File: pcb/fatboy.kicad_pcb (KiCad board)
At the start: 2 copper layers, 232.2 x 108.2 mm, 78 parts, among them J1 Conn_01x04, SW1 SW_Push, U1 Helios

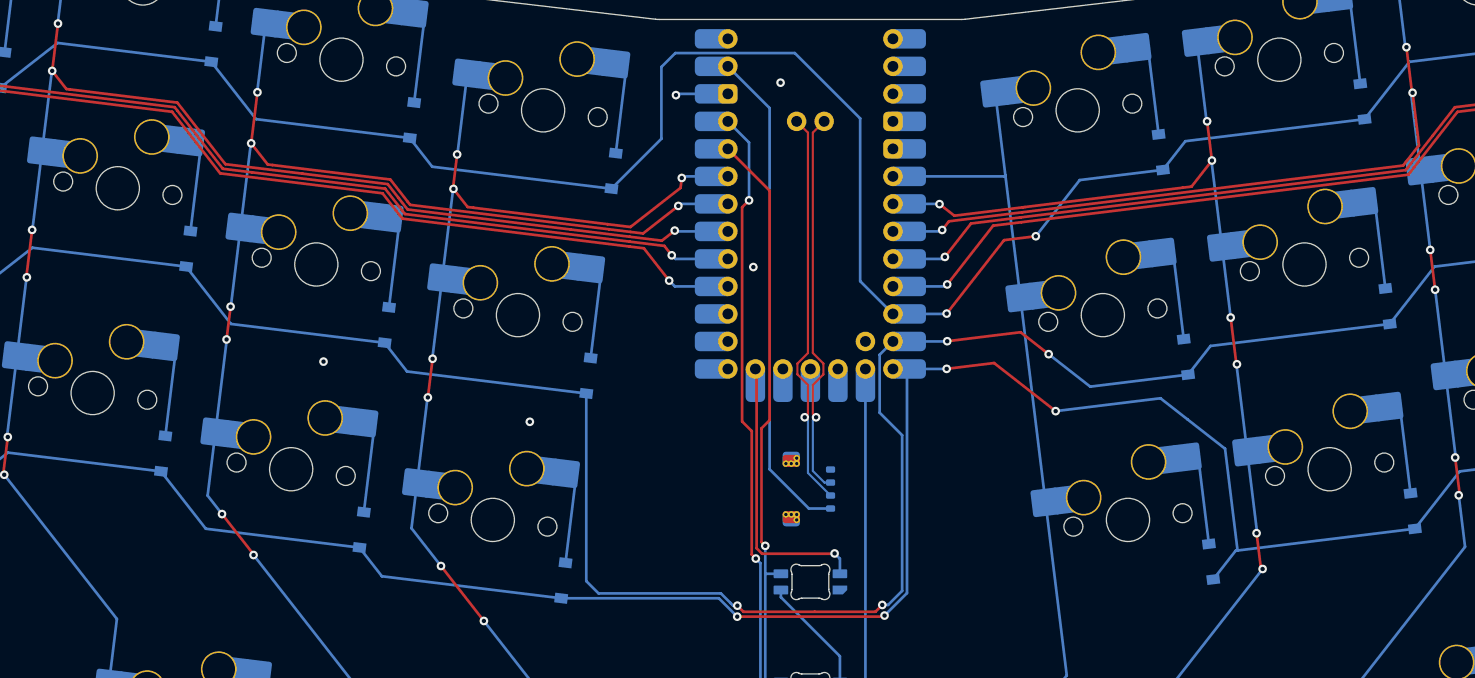
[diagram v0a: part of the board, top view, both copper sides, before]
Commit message: pcb: remove daughterboard
Signed-off-by: Anant Thazhemadam <anant.thazhemadam@gmail.com>
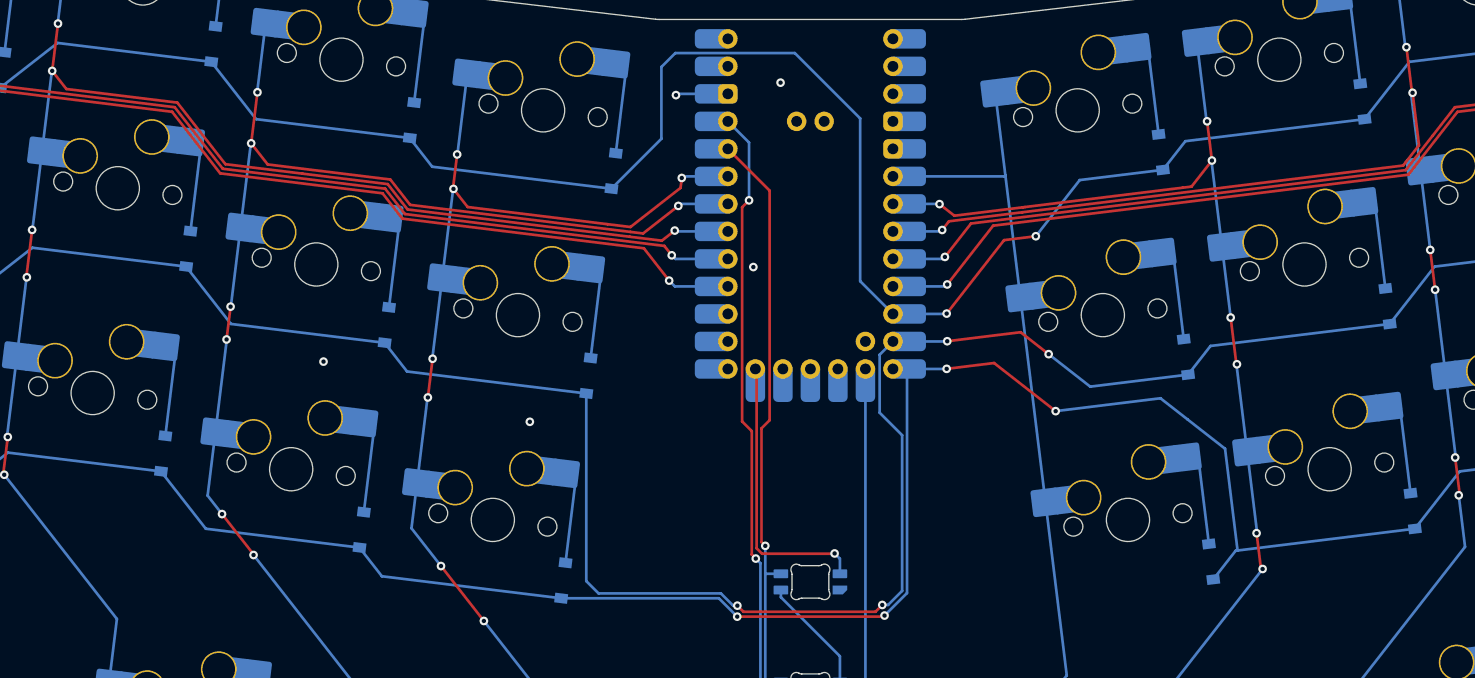
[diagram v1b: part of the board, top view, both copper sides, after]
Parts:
- removed J1: Conn_01x04, fatboy:Molex_Pico-EZmate_78171-0004_1x04-1MP_P1.20mm_Vertical
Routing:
- net 5V: track 45.9 -> 0.00 mm
- net D-: track 36.9 -> 0.00 mm, vias 1 -> 0
- net D+: track 35.8 -> 0.00 mm, vias 1 -> 0

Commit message: pcb: remove jlcjlcjlcjlc on the back of pcb
Signed-off-by: Anant Thazhemadam <anant.thazhemadam@gmail.com>
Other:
- board text removed: "JLCJLCJLCJLC"
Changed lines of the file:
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@@
 		(layer "Edge.Cuts")
-	)
-	(gr_text "JLCJLCJLCJLC"
-		(at 195.675 119.45 90)
-		(layer "B.SilkS")
-		(effects
-			(font
-				(size 1 1)
-				(thickness 0.15)
-			)
-			(justify mirror)
-		)
 	)
 	(segment

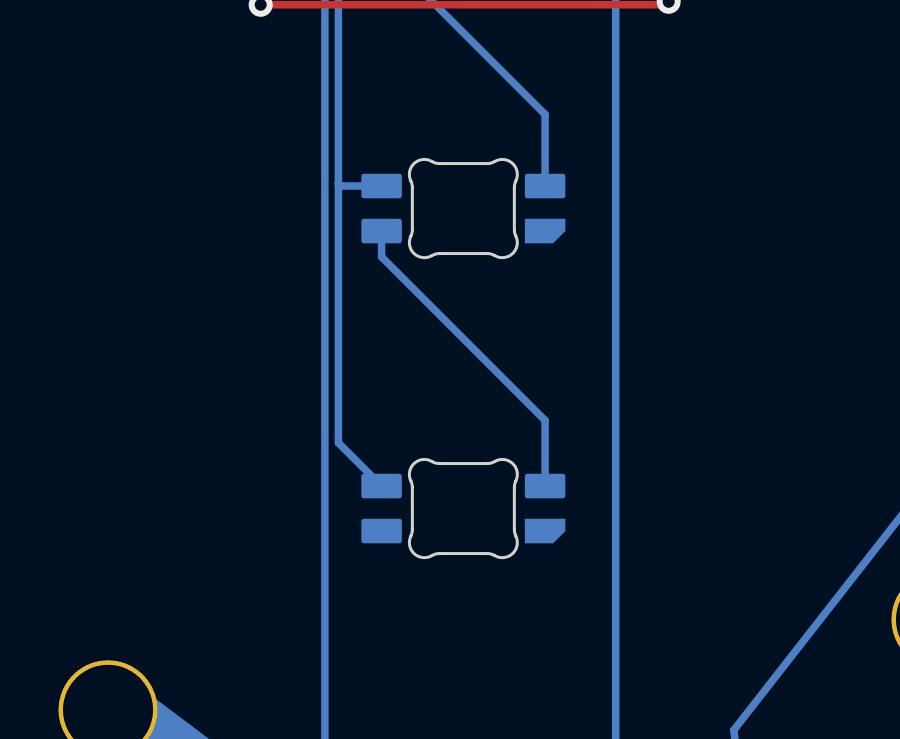
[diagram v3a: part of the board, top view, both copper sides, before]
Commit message: pcb: remove extra led
Signed-off-by: Anant Thazhemadam <anant.thazhemadam@gmail.com>
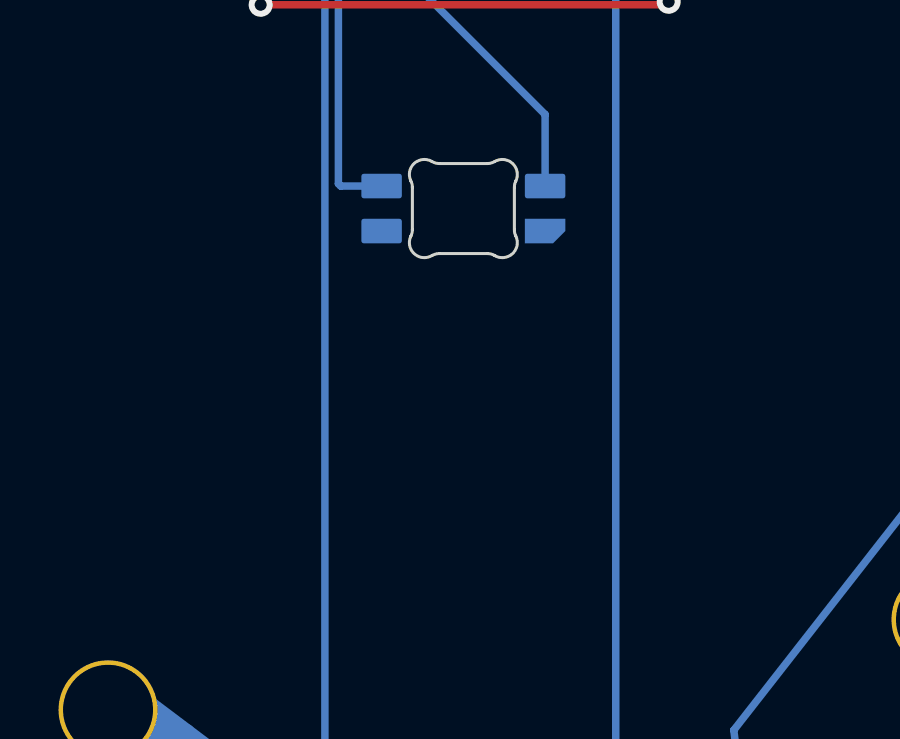
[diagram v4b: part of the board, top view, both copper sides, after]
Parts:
- removed LED3: SK6812MINI-E, fatboy:LED_6028R
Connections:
- LED2 pad 2: Net-(LED2-DOUT) -> unconnected-(LED2-DOUT-Pad2)
- U1 pad 32: D+ -> unconnected-(U1-D+-Pad32)
- U1 pad 33: D- -> unconnected-(U1-D--Pad33)
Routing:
- net Net-(LED2-DOUT): track 10.8 -> 0.00 mm
- net 3V3: track 64.8 -> 54.1 mm

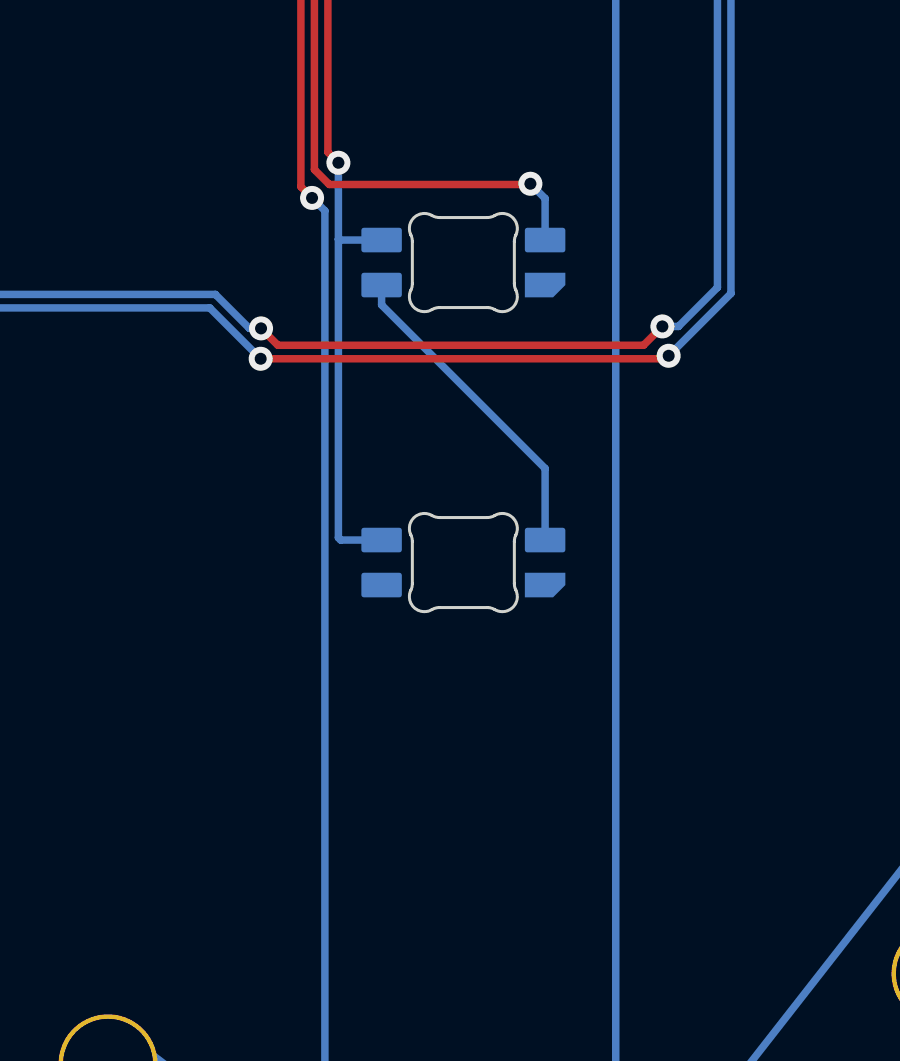
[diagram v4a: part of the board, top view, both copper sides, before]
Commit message: pcb: move down LEDs
Signed-off-by: Anant Thazhemadam <anant.thazhemadam@gmail.com>
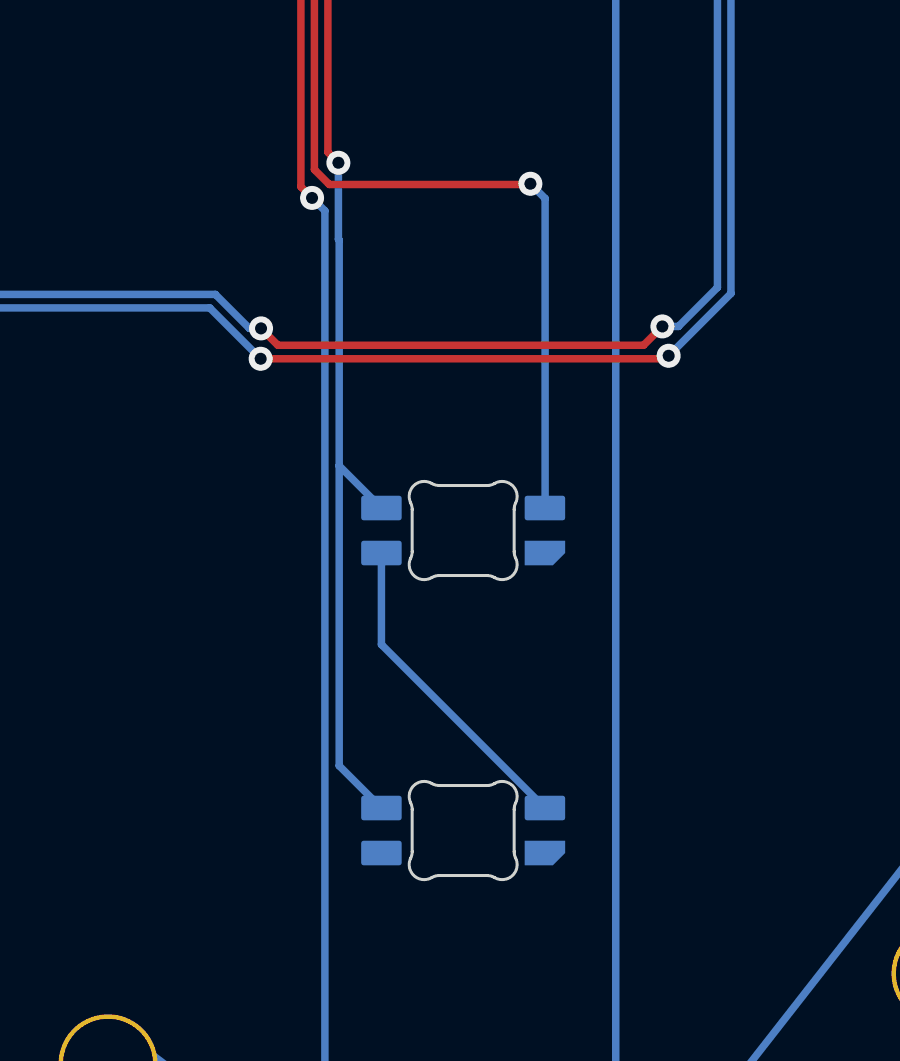
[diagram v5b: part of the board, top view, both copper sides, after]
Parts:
- moved LED1 8.93 mm to (195.8, 161.0)
- moved LED2 8.93 mm to (195.7, 171.0)
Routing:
- net RGB: track 26.1 -> 35.0 mm
- net 3V3: track 54.1 -> 62.8 mm

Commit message: update MX HS SW footprint to PCM_marbastlib-mx:SW_MX_HS_CPG151101S11_1u
Signed-off-by: Anant Thazhemadam <anant.thazhemadam@gmail.com>
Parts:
- D1, D10, D11, D12, D13, D14, D15, D16, D17, D18, D19, D2, D20, D21, D22, D23, D24, D25, D26, D27, D28, D29, D3, D30, D31, D32, D33, D34, D35, D36, D4, D5, D6, D7, D8, D9: footprint fatboy:D_SOD-123 -> Diode_SMD:D_SOD-123
- MX1, MX10, MX11, MX12, MX13, MX14, MX15, MX16, MX17, MX18, MX19, MX2, MX20, MX21, MX22, MX23, MX24, MX25, MX26, MX27, MX28, MX29, MX3, MX30, MX31, MX32, MX33, MX34, MX35, MX36, MX4, MX5, MX6, MX7, MX8, MX9: footprint fatboy:SW_MX_HS_1u -> PCM_marbastlib-mx:SW_MX_HS_CPG151101S11_1u
- U1: footprint fatboy:Helios_ACH -> PCM_marbastlib-xp-promicroish:Helios_ACH

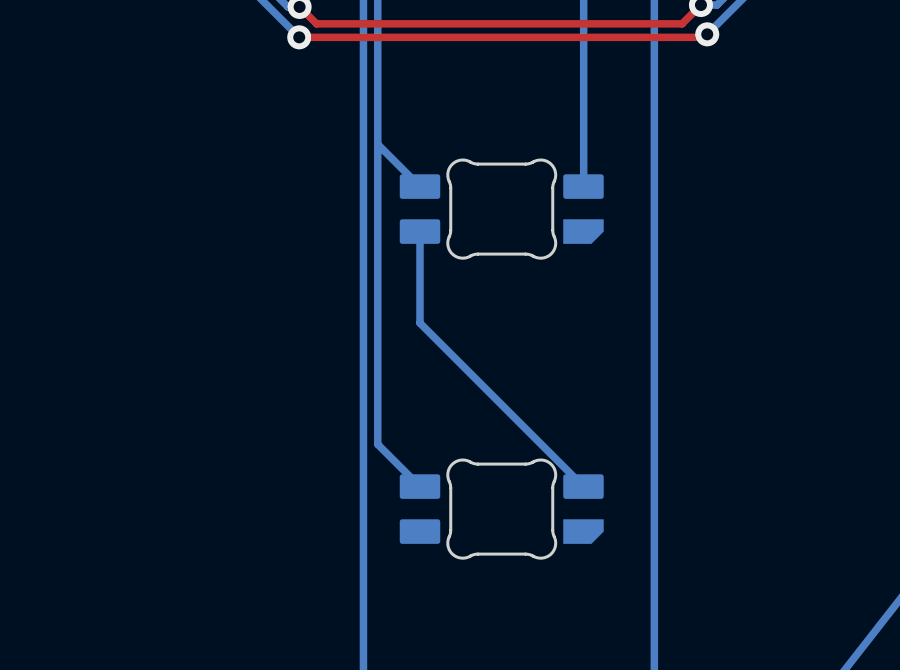
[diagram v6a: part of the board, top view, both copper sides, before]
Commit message: update to use PCM_marbastlib:LED6028R
Signed-off-by: Anant Thazhemadam <anant.thazhemadam@gmail.com>
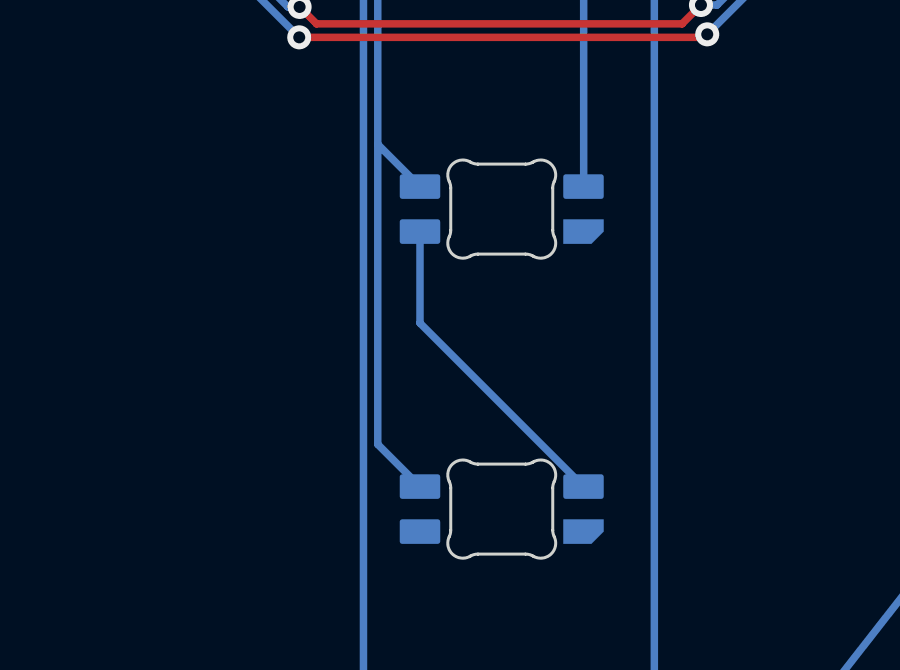
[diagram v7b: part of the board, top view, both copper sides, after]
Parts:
- LED1, LED2: footprint fatboy:LED_6028R -> PCM_marbastlib-various:LED_6028R
